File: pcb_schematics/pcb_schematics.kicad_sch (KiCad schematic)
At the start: 73 parts, among them J1 CUE_SJ1-352XNG, J2 Conn_01x01_Pin, J3 Conn_01x05, J4 Conn_01x05, J5 Conn_01x05, SW1 SW_Push, U1 RPi_Pico_TH, U2 RDA5807M_Module, U3 LM386, U4 LM386

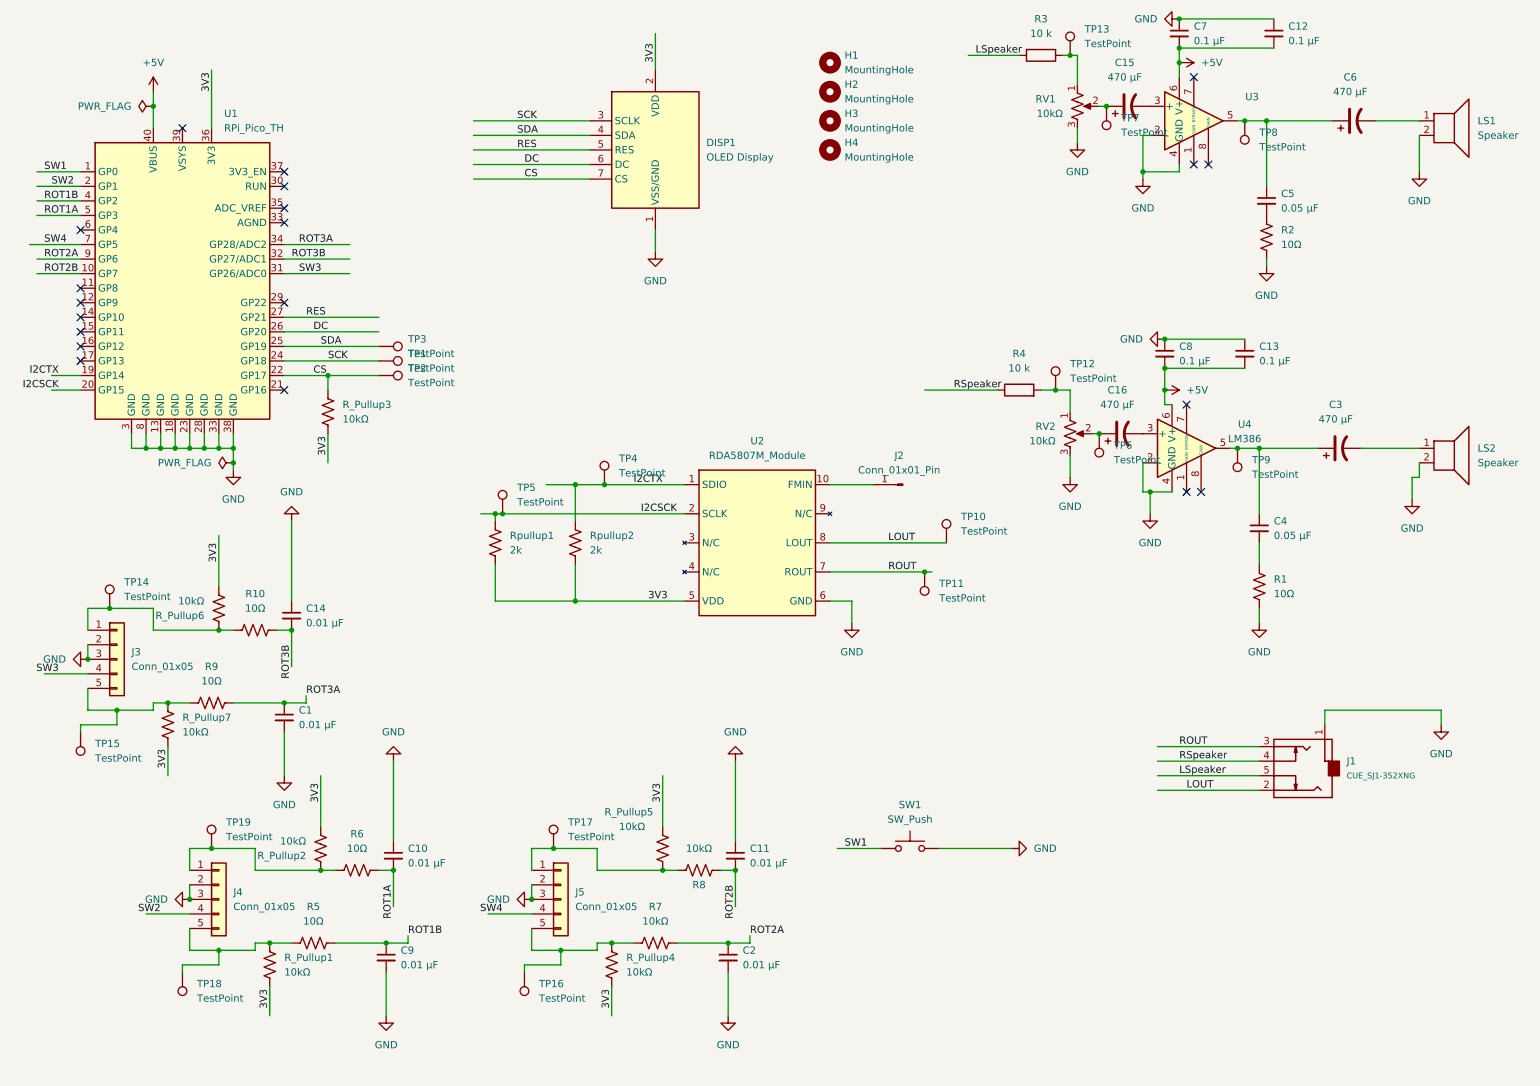
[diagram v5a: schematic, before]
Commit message: Revision 3
Changed the amplifier and the rotary encoder schemtic. Needs work on pcb
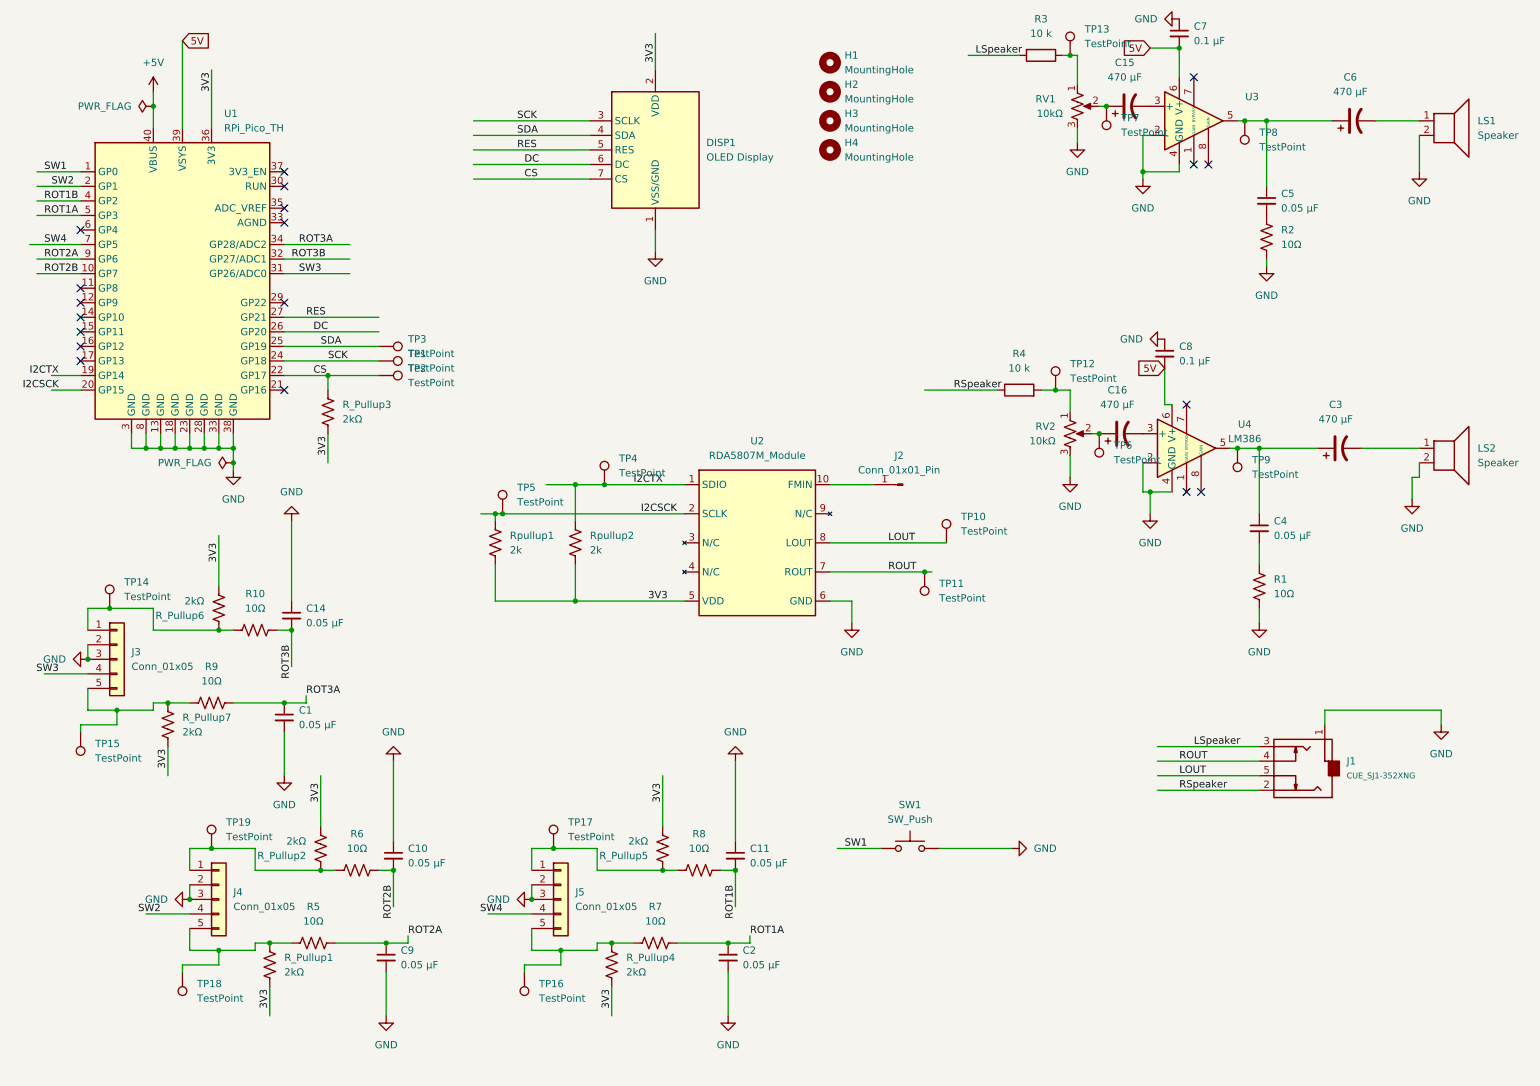
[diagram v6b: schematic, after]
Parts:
- removed C12, C13: 0.1 µF, Capacitor_THT:C_Axial_L3.8mm_D2.6mm_P7.50mm_Horizontal, symbol Device:C_Small
- C1, C10, C11, C14, C2, C9: value 0.01 µF -> 0.05 µF
- J1: footprint Connector_PinHeader_2.54mm:PinHeader_1x05_P2.54mm_Vertical -> ECE:CUE_SJ1-352XNG
- J3, J4, J5: footprint Connector_PinHeader_2.54mm:PinHeader_1x05_P2.54mm_Vertical -> Connector_PinHeader_2.00mm:PinHeader_1x05_P2.00mm_Vertical
- R3, R4: footprint Resistor_THT:R_Axial_DIN0207_L6.3mm_D2.5mm_P10.16mm_Horizontal -> (none)
- R7, R8: value 10kΩ -> 10Ω
- R_Pullup1, R_Pullup2, R_Pullup3, R_Pullup4, R_Pullup5, R_Pullup6, R_Pullup7: value 10kΩ -> 2kΩ
- SW1: footprint Connector_PinHeader_2.54mm:PinHeader_1x02_P2.54mm_Vertical -> Connector_PinHeader_1.27mm:PinHeader_1x02_P1.27mm_Vertical
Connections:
- net +5V: no longer C7.2, C8.2, U3.6 (V+), U4.6 (V+)
- net LOUT: now also J1.5 (Ring_Switch); no longer J1.2 (Tip)
- net LSpeaker: now also J1.3 (Tip); no longer J1.5 (Ring_Switch)
- net ROT1A: now also C2.1, R7.2; no longer C10.2, R6.1
- net ROT1B: now also C11.2, R8.1; no longer C9.1, R5.2
- net ROT2A: now also C9.1, R5.2; no longer C2.1, R7.2
- net ROT2B: now also C10.2, R6.1; no longer C11.2, R8.1
- net ROUT: now also J1.4 (Tip_Switch); no longer J1.3 (Tip)
- net RSpeaker: now also J1.2 (Tip); no longer J1.4 (Tip_Switch)
- net 5V: now reaches U1.39 (VSYS)
- net 5V: now also C7.2, C8.2, U3.6 (V+), U4.6 (V+)
- no-connect marks 20 -> 19
